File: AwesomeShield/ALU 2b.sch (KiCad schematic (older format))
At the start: 82 parts, among them J1 CONN_01X04, J2 CONN_01X04, J3 CONN_01X03, J4 CONN_01X08, J5 CONN_01X01, J6 CONN_01X04, U1 74LS08, U10 LM101, U2 74LS08, U3 74LS08, U4 74LS83, U5 74LS83, U6 74LS83, U7 74LS244, U8 LM101, U9 LM101

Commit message: Added pcb file for shield
Assigned remaining footprints and made first layout iteration
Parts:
- removed U10, U8, U9: LM101, Housings_DIP:DIP-4_W7.62mm_Socket_LongPads, symbol LM101
- added U10, U8, U9: LM741, Housings_DIP:DIP-8_W7.62mm_Socket_LongPads, symbol LM741-RESCUE-ALU_2b
- U1, U2, U3: symbol 74LS08 -> 74LS08-RESCUE-ALU_2b
- U4, U5, U6: symbol 74LS83 -> 74LS83-RESCUE-ALU_2b
- U7: symbol 74LS244 -> 74LS244-RESCUE-ALU_2b
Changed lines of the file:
@@
 EESchema Schematic File Version 2
+LIBS:ALU 2b-rescue
 LIBS:power
 LIBS:device
@@
 LIBS:contrib
 LIBS:valves
+LIBS:ALU 2b-cache
 EELAYER 25 0
 EELAYER END
@@
 $EndDescr
 $Comp
-L 74LS83 U4
+L 74LS83-RESCUE-ALU_2b U4
 U 1 1 59E90E55
 P 5800 1250
@@
 $EndComp
 $Comp
-L 74LS83 U5
+L 74LS83-RESCUE-ALU_2b U5
 U 1 1 59E90F58
 P 5800 3000
@@
 $EndComp
 $Comp
-L 74LS83 U6
+L 74LS83-RESCUE-ALU_2b U6
 U 1 1 59E90F89
 P 5800 4750
@@
 $EndComp
 $Comp
-L 74LS08 U1
+L 74LS08-RESCUE-ALU_2b U1
 U 1 1 59E90FBE
 P 2500 1200
@@
 $EndComp
 $Comp
-L 74LS08 U1
+L 74LS08-RESCUE-ALU_2b U1
 U 2 1 59E91053
 P 2500 1800
@@
 $EndComp
 $Comp
-L 74LS08 U1
+L 74LS08-RESCUE-ALU_2b U1
 U 3 1 59E91098
 P 2500 2400
@@
 $EndComp
 $Comp
-L 74LS08 U1
+L 74LS08-RESCUE-ALU_2b U1
 U 4 1 59E910BB
 P 2500 3000
@@
 $EndComp
 $Comp
-L 74LS08 U2
+L 74LS08-RESCUE-ALU_2b U2
 U 1 1 59E910E4
 P 2500 3600
@@
 $EndComp
 $Comp
-L 74LS08 U2
+L 74LS08-RESCUE-ALU_2b U2
 U 2 1 59E9110D
 P 2500 4200
@@
 $EndComp
 $Comp
-L 74LS08 U2
+L 74LS08-RESCUE-ALU_2b U2
 U 3 1 59E91134
 P 2500 4850
@@
 $EndComp
 $Comp
-L 74LS08 U2
+L 74LS08-RESCUE-ALU_2b U2
 U 4 1 59E91161
 P 2500 5500
@@
 $EndComp
 $Comp
-L 74LS08 U3
+L 74LS08-RESCUE-ALU_2b U3
 U 1 1 59E91192
 P 2500 6100
@@
 $EndComp
 $Comp
-L 74LS08 U3
+L 74LS08-RESCUE-ALU_2b U3
 U 2 1 59E911BF
 P 2500 6700
@@
 $EndComp
 $Comp
-L 74LS08 U3
+L 74LS08-RESCUE-ALU_2b U3
 U 3 1 59E91204
 P 2500 7300
@@
 $EndComp
 $Comp
-L 74LS08 U3
+L 74LS08-RESCUE-ALU_2b U3
 U 4 1 59E91253
 P 2500 7950
@@
 OUTPUT
 $Comp
-L 74LS244 U7
+L 74LS244-RESCUE-ALU_2b U7
 U 1 1 59E9139F
 P 8550 1400
@@
 Text Label 200  7700 0    60   ~ 0
 White_LED
-$Comp
-L LM101 U9
-U 1 1 59EB6431
-P -2000 1700
-F 0 "U9" H -1950 1950 50  0000 L CNN
-F 1 "LM101" H -1950 1850 50  0000 L CNN
-F 2 "Housings_DIP:DIP-4_W7.62mm_Socket_LongPads" H -1950 1750 50  0001 C CNN
-F 3 "" H -1950 1850 50  0001 C CNN
-	1    -2000 1700
-	1    0    0    -1
-$EndComp
 Text Label -3650 2600 1    60   ~ 0
 Using_Op-amp_as_Footprint_For_Switch
@@
 Connection ~ -2350 1600
 $Comp
-L LM101 U8
-U 1 1 59EC7F43
-P -2350 150
-F 0 "U8" H -2300 400 50  0000 L CNN
-F 1 "LM101" H -2300 300 50  0000 L CNN
-F 2 "Housings_DIP:DIP-4_W7.62mm_Socket_LongPads" H -2300 200 50  0001 C CNN
-F 3 "" H -2300 300 50  0001 C CNN
-	1    -2350 150
-	1    0    0    -1
-$EndComp
-$Comp
 L R R20
 U 1 1 59EC811E
@@
 Connection ~ -2350 1300
 Connection ~ -2650 450
-$Comp
-L LM101 U10
-U 1 1 59ECBA58
-P -1850 6800
-F 0 "U10" H -1800 7050 50  0000 L CNN
-F 1 "LM101" H -1800 6950 50  0000 L CNN
-F 2 "Housings_DIP:DIP-4_W7.62mm_Socket_LongPads" H -1800 6850 50  0001 C CNN
-F 3 "" H -1800 6950 50  0001 C CNN
-	1    -1850 6800
-	1    0    0    -1
-$EndComp
 $Comp
 L R R27
@@
 	5100 2550 5000 2550
 Connection ~ 5000 2550
+$Comp
+L LM741-RESCUE-ALU_2b U9
+U 1 1 59E9C8FB
+P -2000 1700
+F 0 "U9" H -2000 1950 50  0000 L CNN
+F 1 "LM741" H -2000 1850 50  0000 L CNN
+F 2 "Housings_DIP:DIP-8_W7.62mm_Socket_LongPads" H -1950 1750 50  0001 C CNN
+F 3 "" H -1850 1850 50  0001 C CNN
+	1    -2000 1700
+	1    0    0    -1
+$EndComp
+$Comp
+L LM741-RESCUE-ALU_2b U8
+U 1 1 59E9DDAE
+P -2350 150
+F 0 "U8" H -2350 400 50  0000 L CNN
+F 1 "LM741" H -2350 300 50  0000 L CNN
+F 2 "Housings_DIP:DIP-8_W7.62mm_Socket_LongPads" H -2300 200 50  0001 C CNN
+F 3 "" H -2200 300 50  0001 C CNN
+	1    -2350 150
+	1    0    0    -1
+$EndComp
+$Comp
+L LM741-RESCUE-ALU_2b U10
+U 1 1 59E9E400
+P -1850 6800
+F 0 "U10" H -1850 7050 50  0000 L CNN
+F 1 "LM741" H -1850 6950 50  0000 L CNN
+F 2 "Housings_DIP:DIP-8_W7.62mm_Socket_LongPads" H -1800 6850 50  0001 C CNN
+F 3 "" H -1700 6950 50  0001 C CNN
+	1    -1850 6800
+	1    0    0    -1
+$EndComp
 $EndSCHEMATC

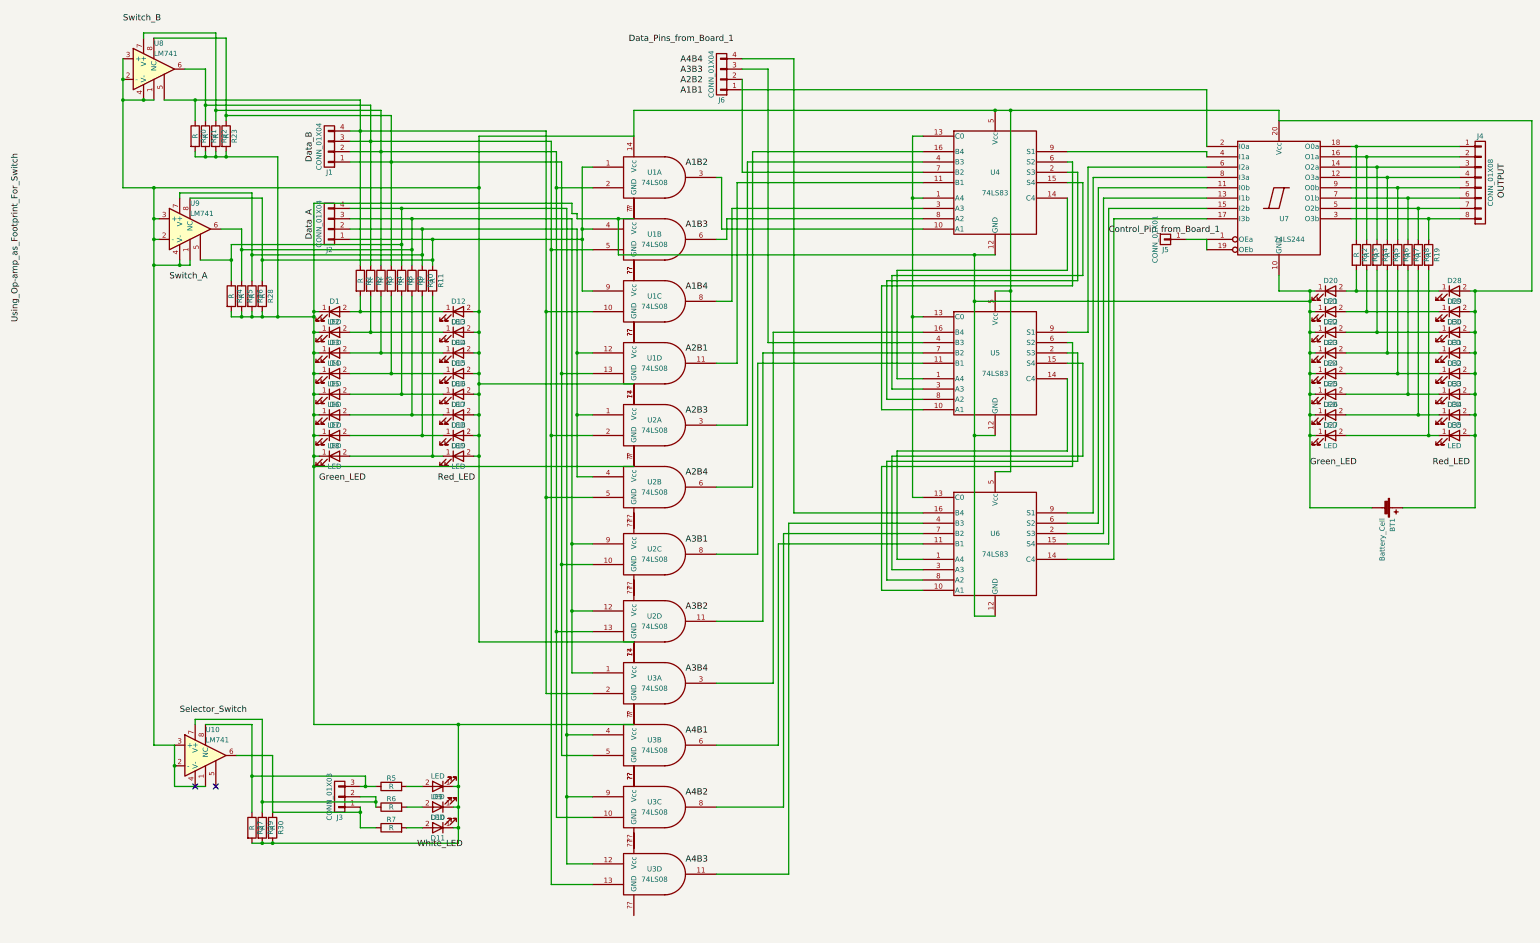
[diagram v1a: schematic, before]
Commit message: Moved the via under the ICs
Vias under the IC were causing short as discovered upon fabrication of the board.
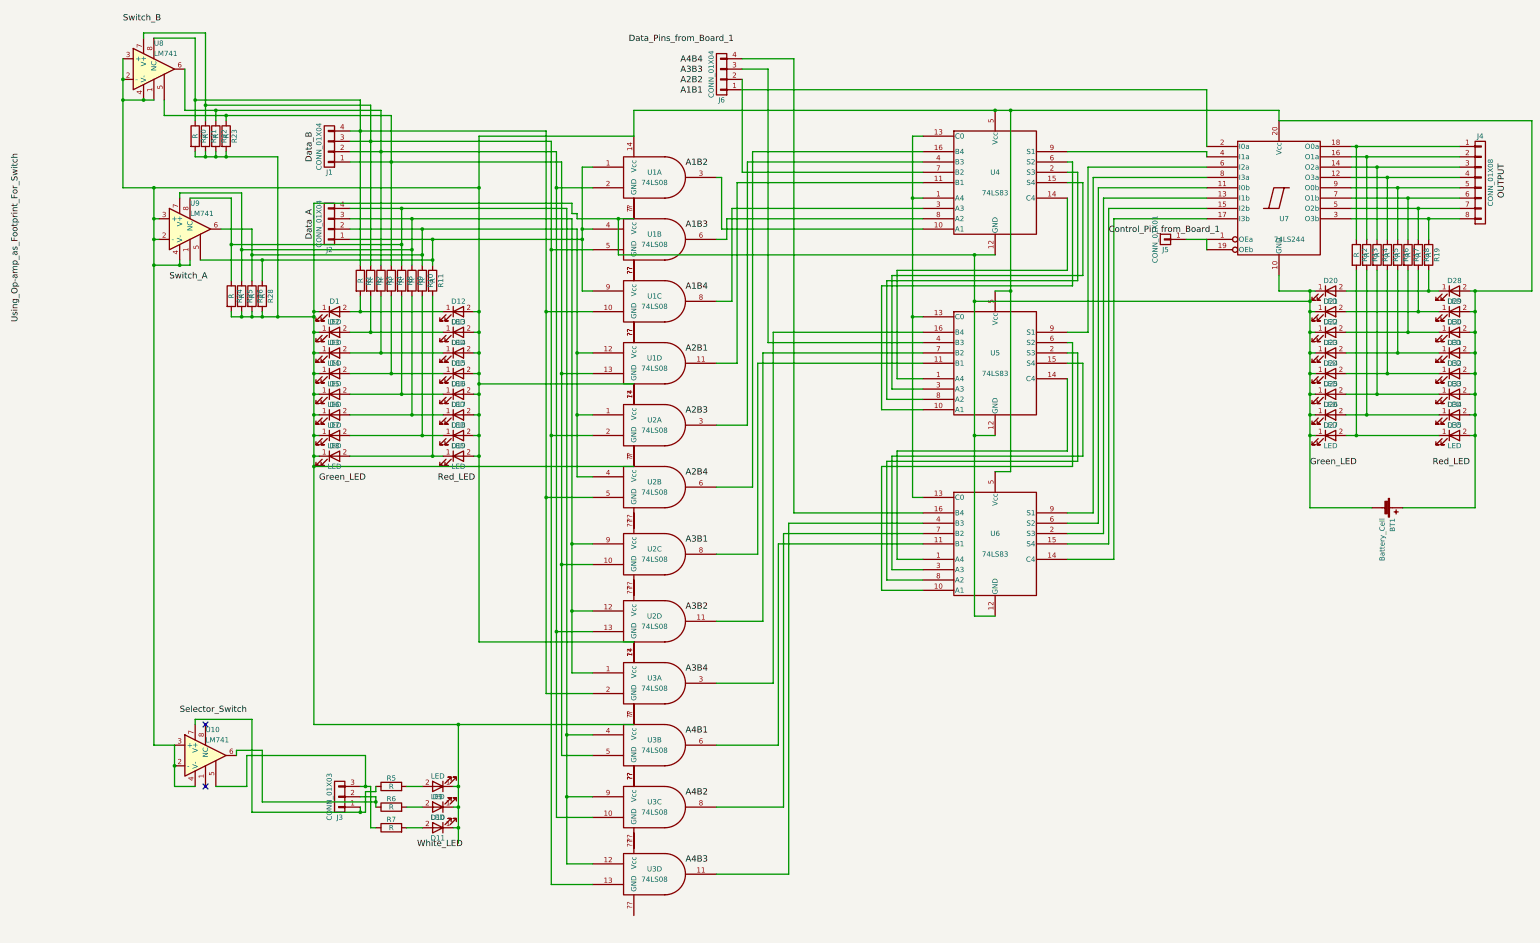
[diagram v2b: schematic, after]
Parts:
- removed R27, R29, R30: R, Resistors_SMD:R_1206_HandSoldering, symbol R
- D1, D10, D11, D12, D13, D14, D15, D16, D17, D18, D19, D2, D20, D21, D22, D23, D24, D25, D26, D27, D28, D29, D3, D30, D31, D32, D33, D34, D35, D4, D5, D6, D7, D8, D9: footprint LED_5630 footprint:LED_5630 -> LEDs:LED_1206
- R1, R10, R11, R12, R13, R14, R15, R16, R17, R18, R19, R2, R20, R21, R22, R23, R24, R25, R26, R28, R3, R4, R5, R6, R7, R8, R9: footprint Resistors_SMD:R_1206_HandSoldering -> Resistors_SMD:R_1206
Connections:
- net at BT1.1 (+), D12.2 (A), D13.2 (A)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: now also U10.4 (V-); no longer U10.1
- net at J2.1 (P1), R11.1, R28.1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: now also U9.5; no longer U9.8 (NC)
- net at J1.2 (P2), R22.1, R3.1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: now also U8.6; no longer U8.7 (V+)
- net at J1.3 (P3), R2.1, R21.1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: now also U8.7 (V+); no longer U8.6
- net at J1.4 (P4), R1.1, R20.1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: now also U8.8 (NC); no longer U8.5
- net at J2.2 (P2), R10.1, R26.1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: now also U9.6; no longer U9.7 (V+)
- net at J1.1 (P1), R23.1, R4.1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: now also U8.5; no longer U8.8 (NC)
- net at J2.3 (P3), R25.1, R9.1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: now also U9.7 (V+); no longer U9.6
- net at J2.4 (P4), R24.1, R8.1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: now also U9.8 (NC); no longer U9.5
- net at J3.2 (P2), R6.1: now also U10.6; no longer U10.7 (V+)
- net at D20.2 (A), D28.1 (K): now also R19.2; no longer R12.2
- net at D21.2 (A), D29.1 (K): now also R18.2; no longer R13.2
- net at D22.2 (A), D30.1 (K): now also R17.2; no longer R14.2
- net at D23.2 (A), D31.1 (K): now also R16.2; no longer R15.2
- net at D24.2 (A), D32.1 (K): now also R15.2; no longer R16.2
- net at D25.2 (A), D33.1 (K): now also R14.2; no longer R17.2
- net at D26.2 (A), D34.1 (K): now also R13.2; no longer R18.2
- net at D27.2 (A), D35.1 (K): now also R12.2; no longer R19.2
- net at U10.5: now also J3.3 (P3), R7.1
- new net: J3.1 (P1), R5.1, U10.7 (V+)
- now unconnected: U10.8 (NC)

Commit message: Final Design
Final design of both base and shield board which is ready to roll.
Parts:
- BT1: footprint Connectors:bornier2 -> Pin_Headers:Pin_Header_Straight_1x02_Pitch2.54mm
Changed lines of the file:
@@
 F 0 "BT1" H 9650 4500 50  0000 L CNN
 F 1 "Battery_Cell" H 9650 4400 50  0000 L CNN
-F 2 "Connectors:bornier2" V 9550 4460 50  0001 C CNN
+F 2 "Pin_Headers:Pin_Header_Straight_1x02_Pitch2.54mm" V 9550 4460 50  0001 C CNN
 F 3 "" V 9550 4460 50  0001 C CNN
 	1    9550 4400
